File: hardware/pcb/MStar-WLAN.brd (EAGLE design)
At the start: 78.7 x 53.7 mm, 43 parts, among them J1 Kobiconn 154-UL6661, J3 DX07S016JA1R1500, Q1 VP2106, Q2 TN0606

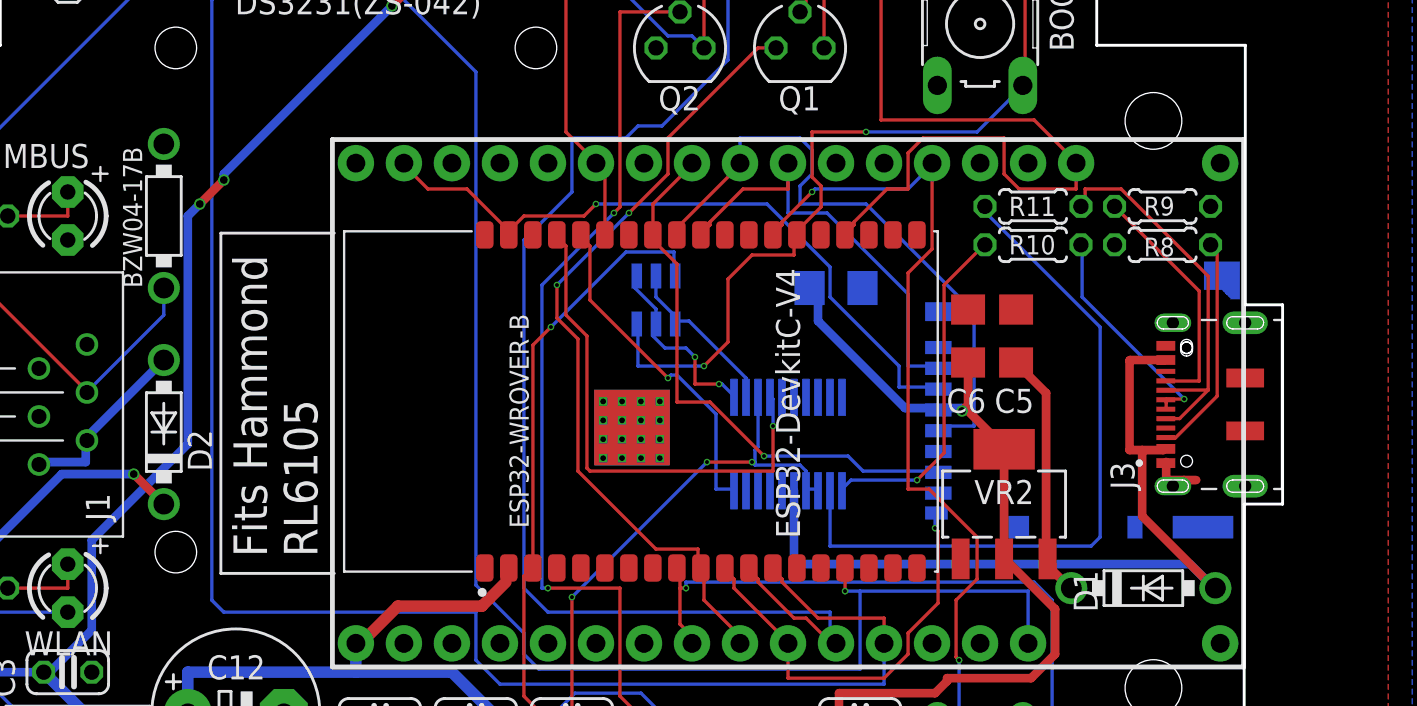
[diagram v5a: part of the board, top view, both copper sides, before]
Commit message: hardware, configurable hostname
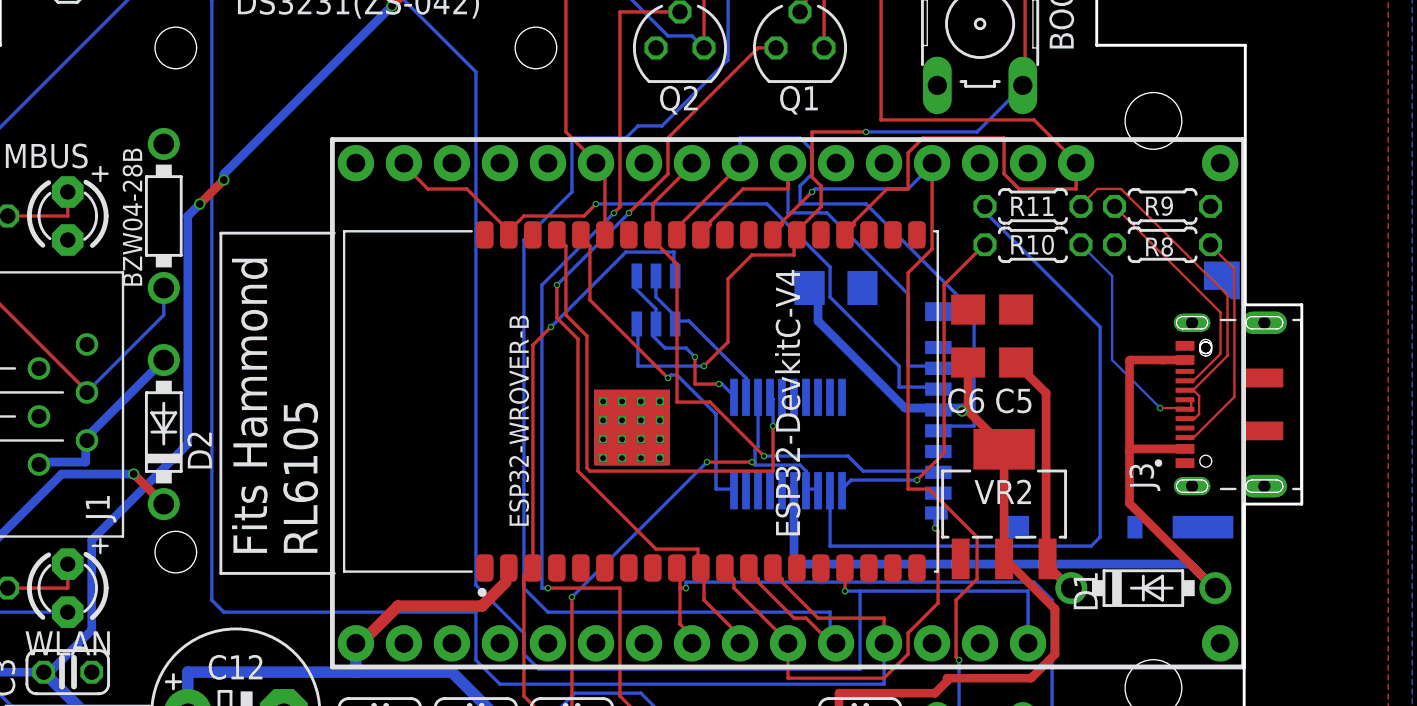
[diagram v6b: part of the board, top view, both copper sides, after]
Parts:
- moved J3 1.02 mm to (71.6, 26.9)
- renumbered BZW04-17B to BZW04-28B
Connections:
- net N$6 renamed CC2
- net N$7 renamed CC1
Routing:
- net VBUS: track 44.2 -> 46.6 mm
- net GND: track 5.62 -> 3.38 mm
- net USBD-: track 20.6 -> 19.4 mm
- net USBD+: track 11.9 -> 13.1 mm
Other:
- board size 78.7 x 53.7 mm -> 79.8 x 53.7 mm

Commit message: Hardware update
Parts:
- removed BZW04-28B: TVS-, MStar-WLAN:DO41-7.6:1
- added D3: BZW04-33, diode:DO41Z10
- BOOT, RESET: value (none) -> PTS645SM432LFS
- C12: device rcl:E5-8,5 -> rcl:E5-6
- MBUS: value (none) -> Green
- WLAN: value (none) -> Red
- moved C1 5.59 mm to (18.2, 3.82), turned to 270 degrees
- moved D2 1.27 mm to (16.5, 26.7)
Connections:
- net /MBUS: now also D3.C; no longer BZW04-28B.C
- net GND: now also D3.A; no longer BZW04-28B.A
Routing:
- net WLAN_LED: track 114.1 -> 56.5 mm, vias 1 -> 2
- net RAW12: track 78.9 -> 64.5 mm, vias 1 -> 0
- net N$14: track 9.65 -> 12.3 mm
- net VCC: track 168.6 -> 169.8 mm, vias 5 -> 1
- net N$17: track 13.2 -> 14.2 mm
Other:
- board text added: "MStar-WLAN mjs 2020.11"
- board text removed: "MStar-WLAN mjs 2020.10"

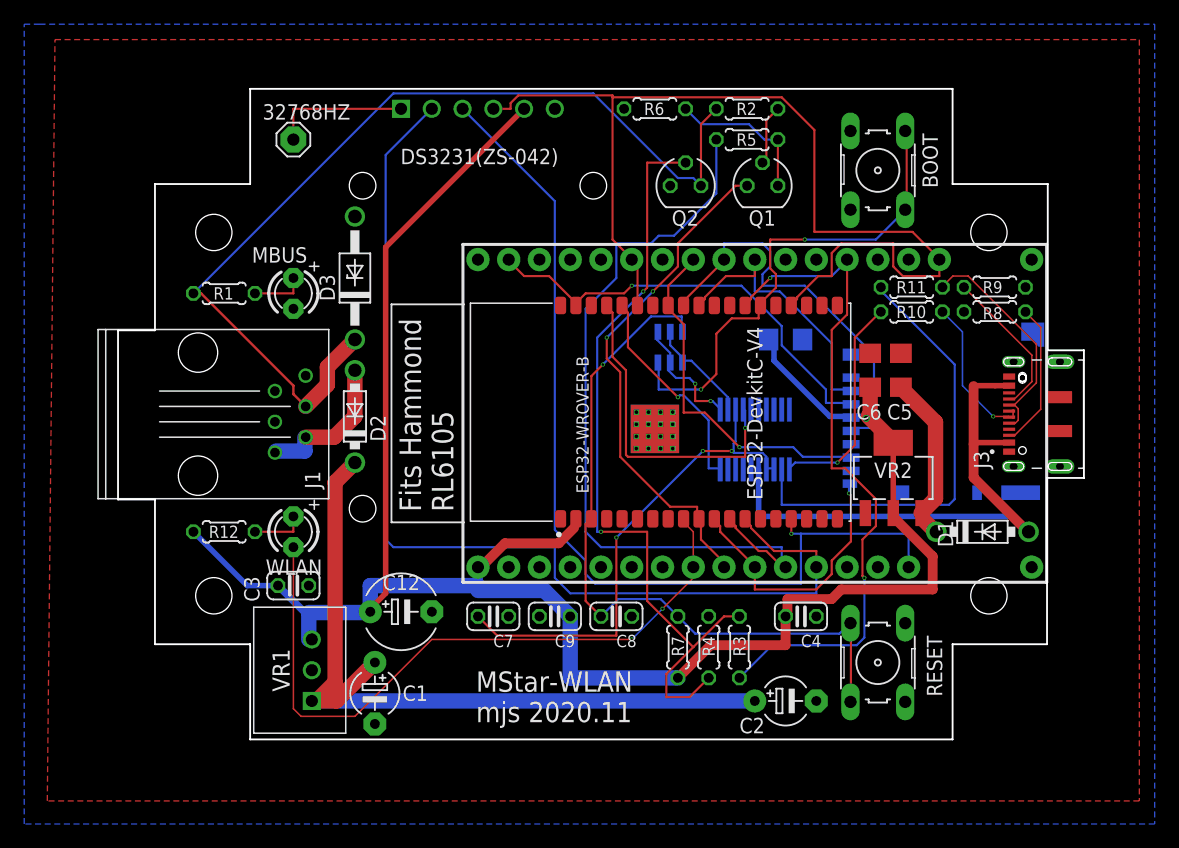
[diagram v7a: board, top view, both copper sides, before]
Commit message: Hardware, charting, much more
Hardware updated for USB-C and to support Devkit-C.
Charting using an RRD database and JavascriptRRD / FLOT.
Show temperature in C or F on /status page.
Configurable logging period for traditional log.
Lots of bug fixes and tweaks, especially in Modbus.
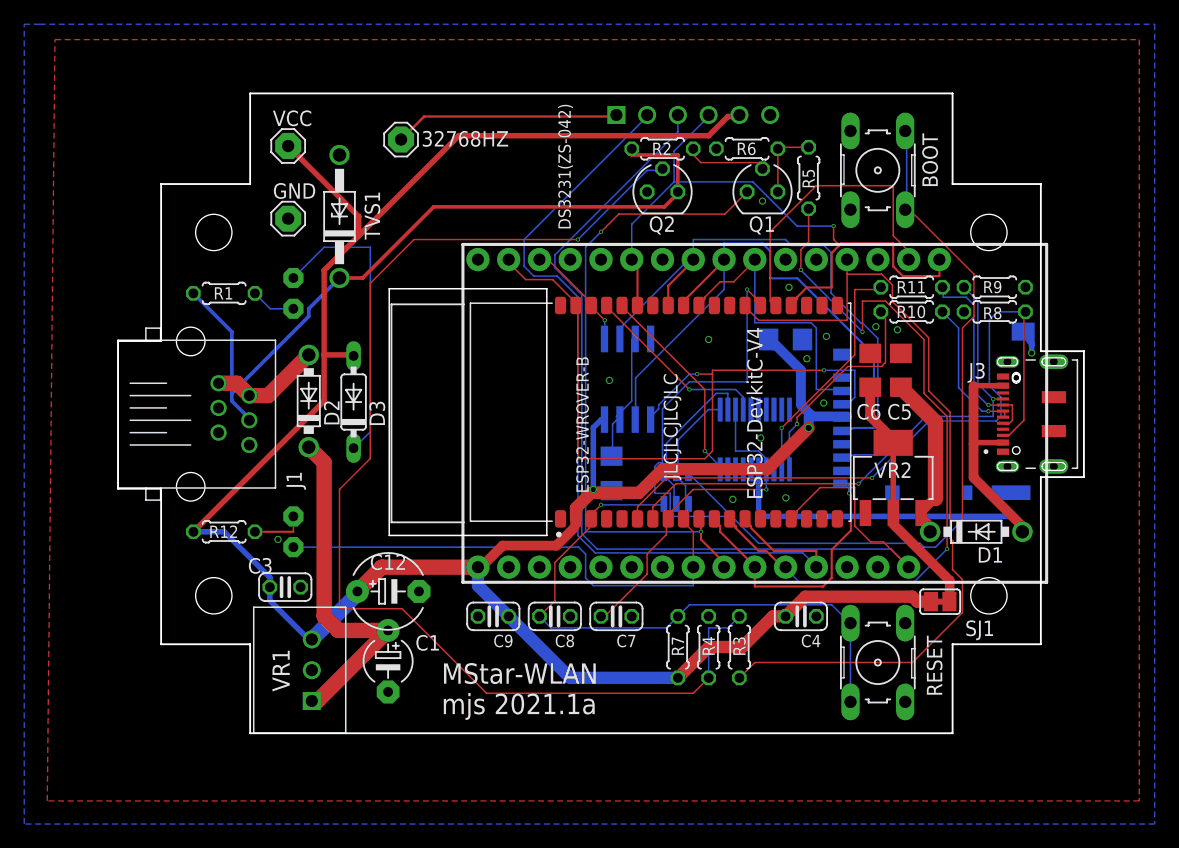
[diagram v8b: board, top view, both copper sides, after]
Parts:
- removed C2: 4m7/25, MStar-WLAN:E5-4
- added GND, VCC: MCS10B, MStar-WLAN:MCS10B
- added IC1: FRAM, MStar-WLAN:SO-08M
- added R13: 10K, rcl:R1206
- added SJ1: (no value), jumper:SJ
- added TVS1: BZW04-33, diode:DO41Z10
- C1: value 4m7/25 -> 2k2/35
- C12: value 100u -> 2k0/6.3
- D3: value BZW04-33 -> 1N4148; device diode:DO41Z10 -> MStar-WLAN:DO35-7
- J1: value Kobiconn 154-UL6661 -> Kycon GLX-N-66; device MStar-WLAN:RJ12 -> MStar-WLAN:6P6C
- R1, R6: value 10K -> 1K
- moved DS3231(ZS-042) 17.8 mm to (44.5, 33.8)
- moved IMH3A 11.7 mm to (43.0, 20.7), turned to 90 degrees
- moved D3 10.2 mm to (16.4, 27.9)
- moved C7 10.2 mm to (38.1, 10.2)
- moved 32768HZ 8.89 mm to (20.3, 49.5)
- moved R6 8.30 mm to (48.9, 48.8)
- moved R2 7.73 mm to (41.9, 48.8)
- moved R5 5.99 mm to (54.0, 46.4), turned to 90 degrees
- moved C9 5.08 mm to (27.9, 10.2)
- moved C8 5.08 mm to (33.0, 10.2)
- moved D2 4.02 mm to (12.7, 27.9)
- moved C1 2.86 mm to (19.3, 6.46)
- moved C12 1.99 mm to (19.3, 12.2)
- moved Q2 1.97 mm to (41.9, 45.2)
- moved J1 1.52 mm to (2.03, 26.9)
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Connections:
- removed net EXT_5V: U$1.19
- removed net N$15: C7.1, FT231XS.13, FT231XS.14, FT231XS.3
- new net N$6: ESP32-WROVER-B.36, IC1.1, U$1.36
- new net N$7: IC1.3, IC1.7, R13.2
- new net N$8: D3.C, MBUS.A
- new net N$9: ESP32-WROVER-B.24, U$1.24
- new net VCCIO: C7.1, ESP32-WROVER-B.8, FT231XS.13, FT231XS.14, FT231XS.3
- net /MBUS: now also TVS1.C; no longer D3.C
- net CC1: now also ESP32-WROVER-B.6
- net CC2: now also ESP32-WROVER-B.7
- net CLK: now also IC1.6
- net GND: now also GND.MP, IC1.4, TVS1.A; no longer C2.-, D3.A, ESP32-WROVER-B.39, ESP32-WROVER-B.40, ESP32-WROVER-B.P$1, ESP32-WROVER-B.P$10, ESP32-WROVER-B.P$11, ESP32-WROVER-B.P$12, ESP32-WROVER-B.P$13, ESP32-WROVER-B.P$14, ESP32-WROVER-B.P$15, ESP32-WROVER-B.P$16, ESP32-WROVER-B.P$2, ESP32-WROVER-B.P$3, ESP32-WROVER-B.P$4, ESP32-WROVER-B.P$5, ESP32-WROVER-B.P$6, ESP32-WROVER-B.P$7, ESP32-WROVER-B.P$8, ESP32-WROVER-B.P$9, MBUS.K
- net MISO: now also IC1.2
- net MOSI: now also IC1.5
- net N$1: now also MBUS.K; no longer MBUS.A
- net RAW12: no longer C2.+
- net VCC: now also D3.A, IC1.8, R13.1, SJ1.1, SJ1.2, VCC.MP
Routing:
- net VCC: track 169.8 -> 230.3 mm, vias 1 -> 2
- net IO0: track 41.1 -> 94.4 mm
- net CC1: track 12.1 -> 57.0 mm, vias 0 -> 1
- net N$15: track 41.1 -> 0.00 mm, vias 3 -> 0
- net RAW12: track 64.5 -> 29.0 mm
- net N$2: track 64.7 -> 97.0 mm, vias 2 -> 1
- net CC2: track 12.6 -> 44.7 mm, vias 0 -> 2
- net I2C_SDA: track 85.5 -> 54.8 mm, vias 0 -> 1
- net VCCIO: track 0.00 -> 29.9 mm, vias 0 -> 1
- net N$9: track 0.00 -> 24.7 mm
- net N$8: track 0.00 -> 24.6 mm
- net MOSI: track 36.7 -> 60.7 mm, vias 1 -> 2
- net MISO: track 29.4 -> 49.0 mm, vias 1 -> 0
- net USBDM: track 37.4 -> 19.6 mm, vias 0 -> 1
- net CLK: track 33.3 -> 49.0 mm
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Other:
- board size 79.8 x 53.7 mm -> 79.8 x 52.8 mm
- board text added: "JLCJLCJLCJLC"
- board text added: "MStar-WLAN mjs 2021.1a"
- board text removed: "MStar-WLAN mjs 2020.11"
